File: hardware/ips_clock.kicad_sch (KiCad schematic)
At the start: 1 part, among them U1 LUAT-ESP32-C3

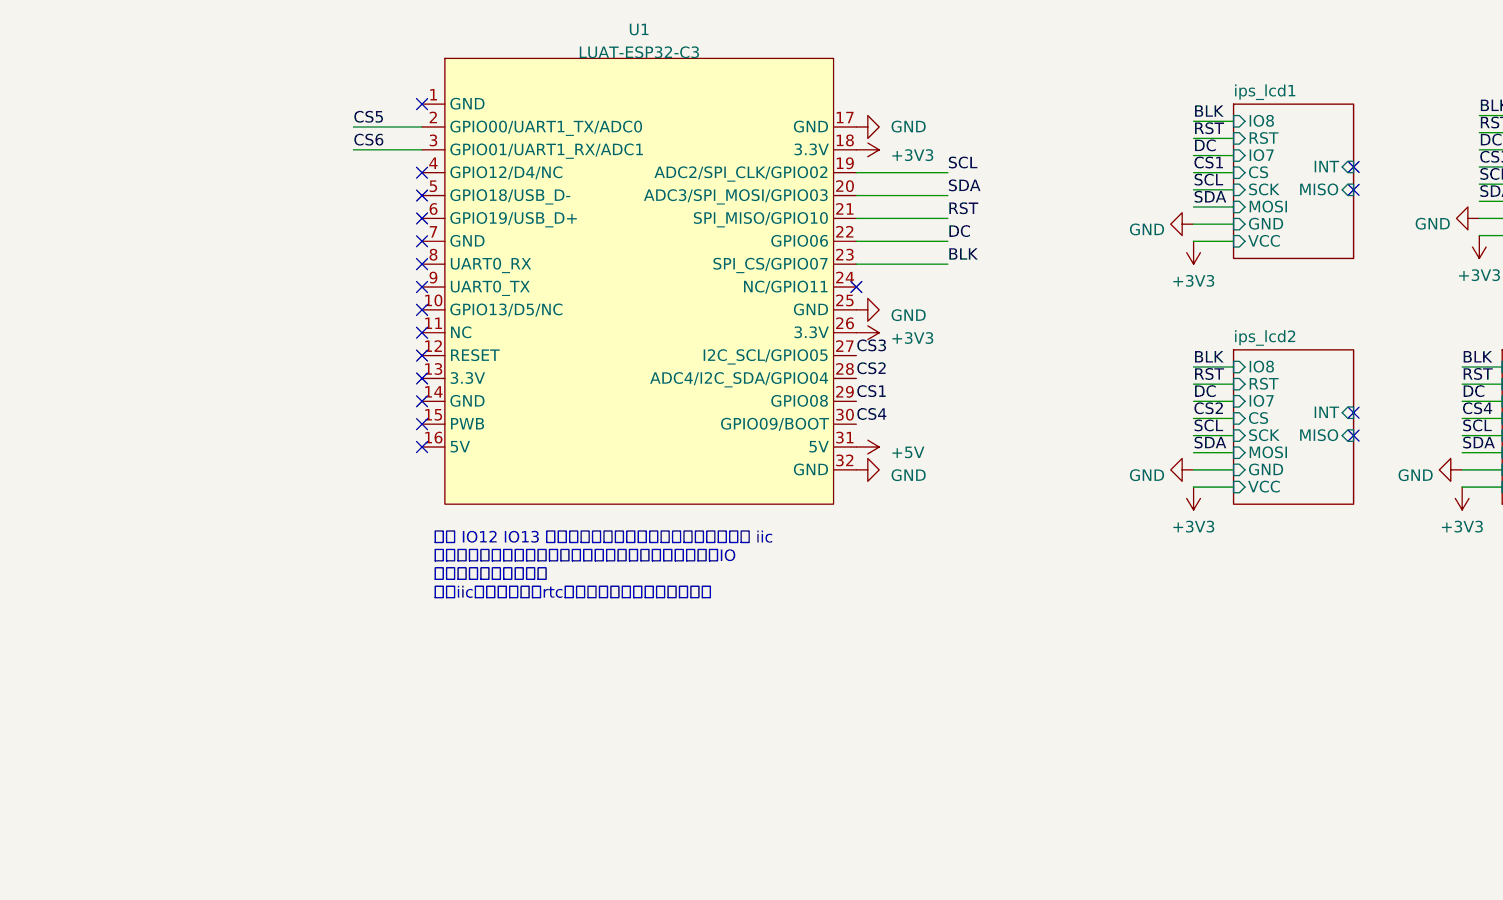
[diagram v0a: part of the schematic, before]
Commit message: 最后更新了PCB的布局
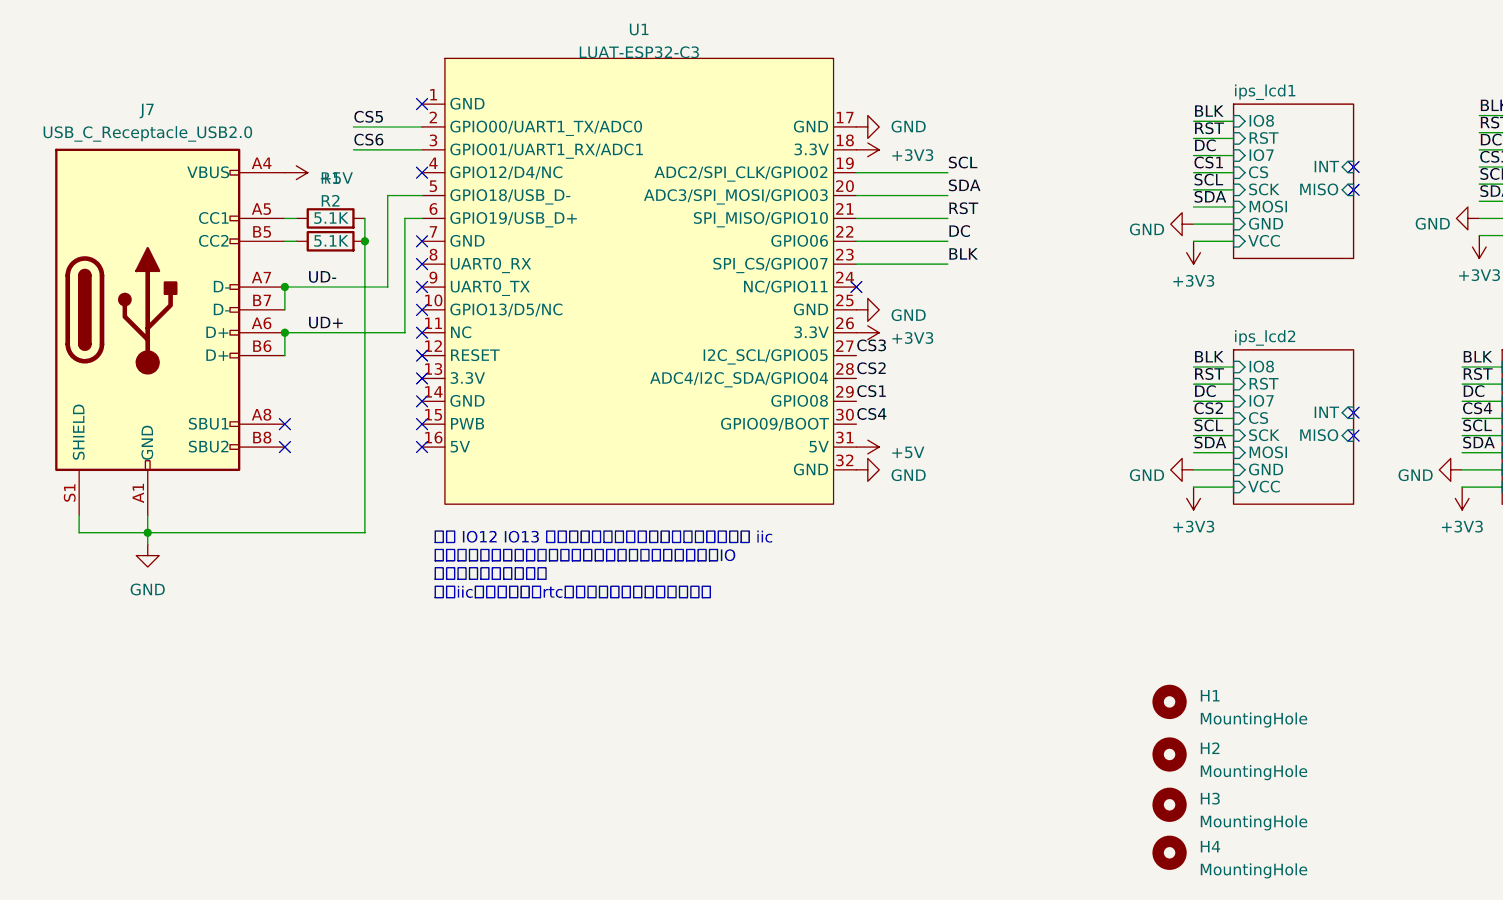
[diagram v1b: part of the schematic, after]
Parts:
- added H1, H2, H3, H4: MountingHole, MountingHole:MountingHole_2.2mm_M2_Pad, symbol Mechanical:MountingHole
- added J7: USB_C_Receptacle_USB2.0, Connector_USB:USB_C_Receptacle_G-Switch_GT-USB-7010ASV, symbol Connector:USB_C_Receptacle_USB2.0
- added R1, R2: 5.1K, Resistor_SMD:R_0603_1608Metric, symbol Device:R
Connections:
- net +5V: now also J7.A4 (VBUS), J7.A9 (VBUS), J7.B4 (VBUS), J7.B9 (VBUS)
- net GND: now also J7.A1 (GND), J7.A12 (GND), J7.B1 (GND), J7.B12 (GND), J7.S1 (SHIELD), R1.2, R2.2
- net UD-: now reaches U1.5 (GPIO18/USB_D-)
- net UD-: now also J7.A7 (D-), J7.B7 (D-)
- net UD+: now reaches U1.6 (GPIO19/USB_D+)
- net UD+: now also J7.A6 (D+), J7.B6 (D+)
- new net: J7.A5 (CC1), R1.1
- new net: J7.B5 (CC2), R2.1

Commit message: 导出了原理图，方便之后在线查看
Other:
- title: (none) -> IPS ESP32C3 联网拟辉光管时钟
- moved on the sheet: H1, H2, H3, H4, J7, R1, R2, U1
